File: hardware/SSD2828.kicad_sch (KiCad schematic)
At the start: 66 parts, among them IC1 TLV62568DBVR, J1 FH35C-25S-0.3SHW_50_, J3 Conn_01x34, U1 PAM2306DYPAA, U1 SSD2828QN4, Y1 24mhz

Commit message: fixed details
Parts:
- J3: footprint Connector_FFC-FPC:FPC_34 -> mylib:FPC_34
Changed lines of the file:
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@@
       (effects (font (size 1.27 1.27)))
     )
-    (property "Footprint" "Connector_FFC-FPC:FPC_34" (at 26.67 74.295 0)
+    (property "Footprint" "mylib:FPC_34" (at 26.67 74.295 0)
       (effects (font (size 1.27 1.27)) hide)
     )
@@
         )
         (path "/e63e39d7-6ac0-4ffd-8aa3-1841a4541b55/eadf4466-e824-4ab1-a46a-9025d68137a1"
-          (reference "R22") (unit 1)
+          (reference "R11") (unit 1)
         )
         (path "/e63e39d7-6ac0-4ffd-8aa3-1841a4541b55/d0befddb-c525-47aa-a36b-f999bfb6acb2"

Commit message: version 1.0
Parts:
- added TP42: (no value), TestPoint:TestPoint_Pad_1.0x1.0mm, symbol Connector:TestPoint_Flag
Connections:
- net at U1.61 (SYS_CLK_OUT): now also TP42.1
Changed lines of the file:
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@@
+    )
+  )
+  (symbol (lib_id "Connector:TestPoint_Flag") (at 156.21 66.675 0) (unit 1)
+    (in_bom yes) (on_board yes) (dnp no)
+    (property "Reference" "TP42" (at 167.64 64.77 0)
+      (effects (font (size 1.27 1.27)) (justify right))
+    )
+    (property "Value" " " (at 154.305 63.373 0)
+      (effects (font (size 1.27 1.27)) (justify right))
+    )
+    (property "Footprint" "TestPoint:TestPoint_Pad_1.0x1.0mm" (at 161.29 66.675 0)
+      (effects (font (size 1.27 1.27)) hide)
+    )
+    (property "Datasheet" "~" (at 161.29 66.675 0)
+      (effects (font (size 1.27 1.27)) hide)
+    )
+    (pin "1")
+    (instances
+      (project "ssd2828_board"
+        (path "/e63e39d7-6ac0-4ffd-8aa3-1841a4541b55/eadf4466-e824-4ab1-a46a-9025d68137a1"
+          (reference "TP42") (unit 1)
+        )
+      )
     )
   )

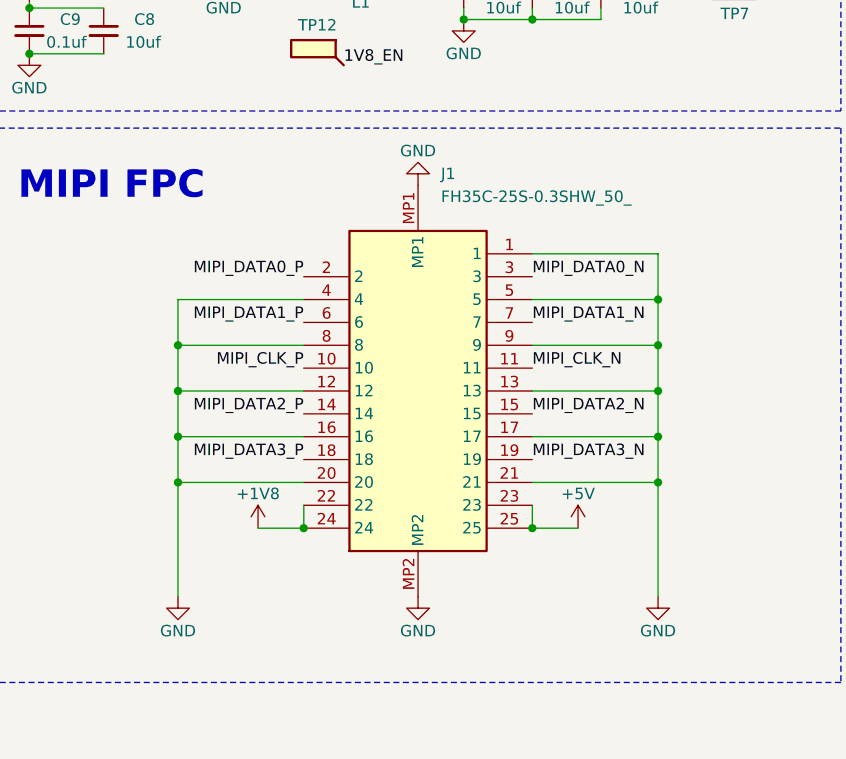
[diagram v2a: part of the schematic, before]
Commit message: fixed hirose FPC connector poinitng backwards on the 2 lcd boards+added stm32f401 boilerplate code
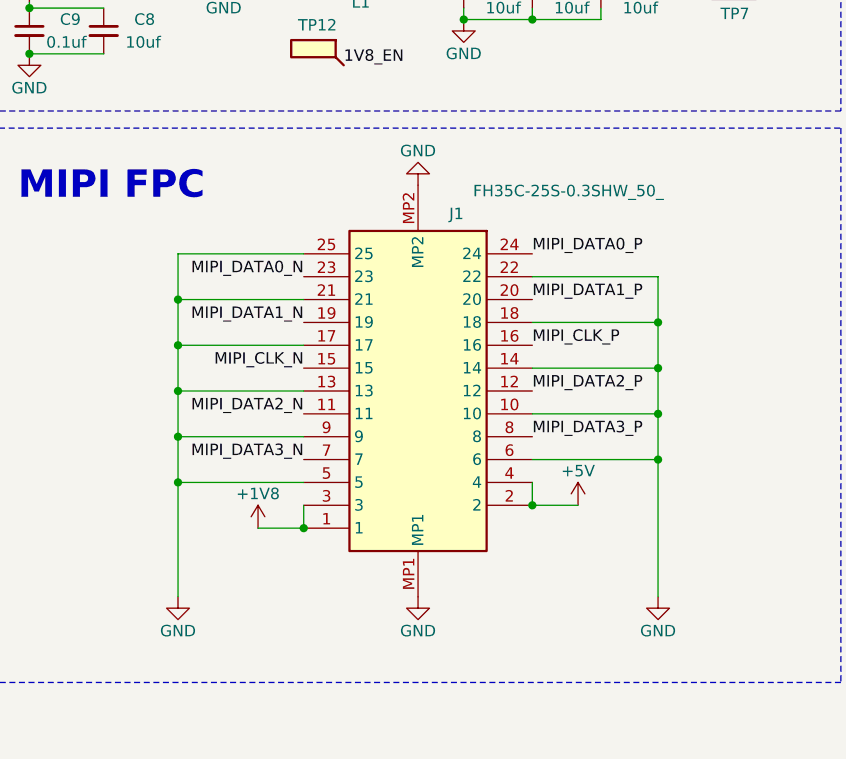
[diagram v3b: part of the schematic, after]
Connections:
- net +1V8: now also J1.1, J1.3; no longer J1.22, J1.24
- net +5V: now also J1.2, J1.4; no longer J1.23, J1.25
- net GND: now also J1.10, J1.14, J1.18, J1.22, J1.25, J1.6; no longer J1.1, J1.12, J1.16, J1.20, J1.4, J1.8
- net MIPI_CLK_N: now also J1.15; no longer J1.11
- net MIPI_CLK_P: now also J1.16; no longer J1.10
- net MIPI_DATA0_N: now also J1.23; no longer J1.3
- net MIPI_DATA0_P: now also J1.24; no longer J1.2
- net MIPI_DATA1_N: now also J1.19; no longer J1.7
- net MIPI_DATA1_P: now also J1.20; no longer J1.6
- net MIPI_DATA2_N: now also J1.11; no longer J1.15
- net MIPI_DATA2_P: now also J1.12; no longer J1.14
- net MIPI_DATA3_N: now also J1.7; no longer J1.19
- net MIPI_DATA3_P: now also J1.8; no longer J1.18
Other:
- moved on the sheet: J1
